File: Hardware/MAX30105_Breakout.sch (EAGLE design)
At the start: 27 parts, among them Q1 200mA/50V, Q2 200mA/50V, U1 1.8V/100mA, U2 MAX30105

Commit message: adding silk labelling
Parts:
- removed JP2: INT, SparkFun-Passives:JUMPER-PAD-2-NC_BY_TRACE
- removed JP3: PU, SparkFun-Passives:JUMPER-PAD-3-NC_BY_TRACE
- removed LOGO1: SFE_LOGO_NAME_FLAME.1_INCH, SparkFun-Aesthetics:SFE_LOGO_NAME_FLAME.1_INCH
- removed LOGO4: SFE_LOGO_FLAME.1EXP, SparkFun-Aesthetics:SFE_LOGO_FLAME.1EXP
- removed STANDOFF1, STANDOFF4: STAND-OFF, SparkFun-Electromechanical:STAND-OFF
- added FID3, FID4: FIDUCIALUFIDUCIAL, SparkFun-Aesthetics:FIDUCIALUFIDUCIAL
- added J1, J3, J4, J5, J6, J7, J8: GATORGATOR_MINI, SparkFun-Connectors:GATORGATOR_MINI
- FID1, FID2: value FIDUCIAL1X2 -> FIDUCIALUFIDUCIAL; device SparkFun-Aesthetics:FIDUCIAL1X2 -> SparkFun-Aesthetics:FIDUCIALUFIDUCIAL
- J2: value (none) -> GATORGATOR_MINI; device SparkFun-Connectors:M05PTH -> SparkFun-Connectors:GATORGATOR_MINI
- R1, R2: value 4.7K -> 10k; device SparkFun-Resistors:4.7KOHM-1/10W-1%(0603) -> SparkFun-Resistors:10KOHM-0603-1/10W-1%
- R8, R9: value 4.7K -> 2.2k; device SparkFun-Resistors:4.7KOHM-1/10W-1%(0603) -> SparkFun-Resistors:2.2KOHM-0603-1/10W-1%
- U2: value MAX30105 -> 30102; device SparkFun-Sensors:MAX30105SMD -> SparkFun-Sensors:MAX3010X-30102
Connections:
- removed net 5V: C1.1, C5.1, J2.3, JP2.2, JP3.2, U1.EN, U1.IN, U2.VLED+@10, U2.VLED+@9
- removed net N$1: JP2.1, R5.2
- removed net N$2: JP3.1, R2.2
- removed net N$3: JP3.3, R1.2
- new net 3.3V: C1.1, C5.1, J2.P$1, J6.P$1, R1.2, R2.2, R5.2, U1.EN, U1.IN, U2.VLED+@10, U2.VLED+@9
- net !INT: no longer J2.5
- net GND: now also J1.P$1, J5.P$1; no longer J2.4
- net SCL: now also J4.P$1, J8.P$1; no longer J2.1
- net SDA: now also J3.P$1, J7.P$1; no longer J2.2
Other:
- note removed: "Clear Jumper to remove I2C Pull-ups from bus"

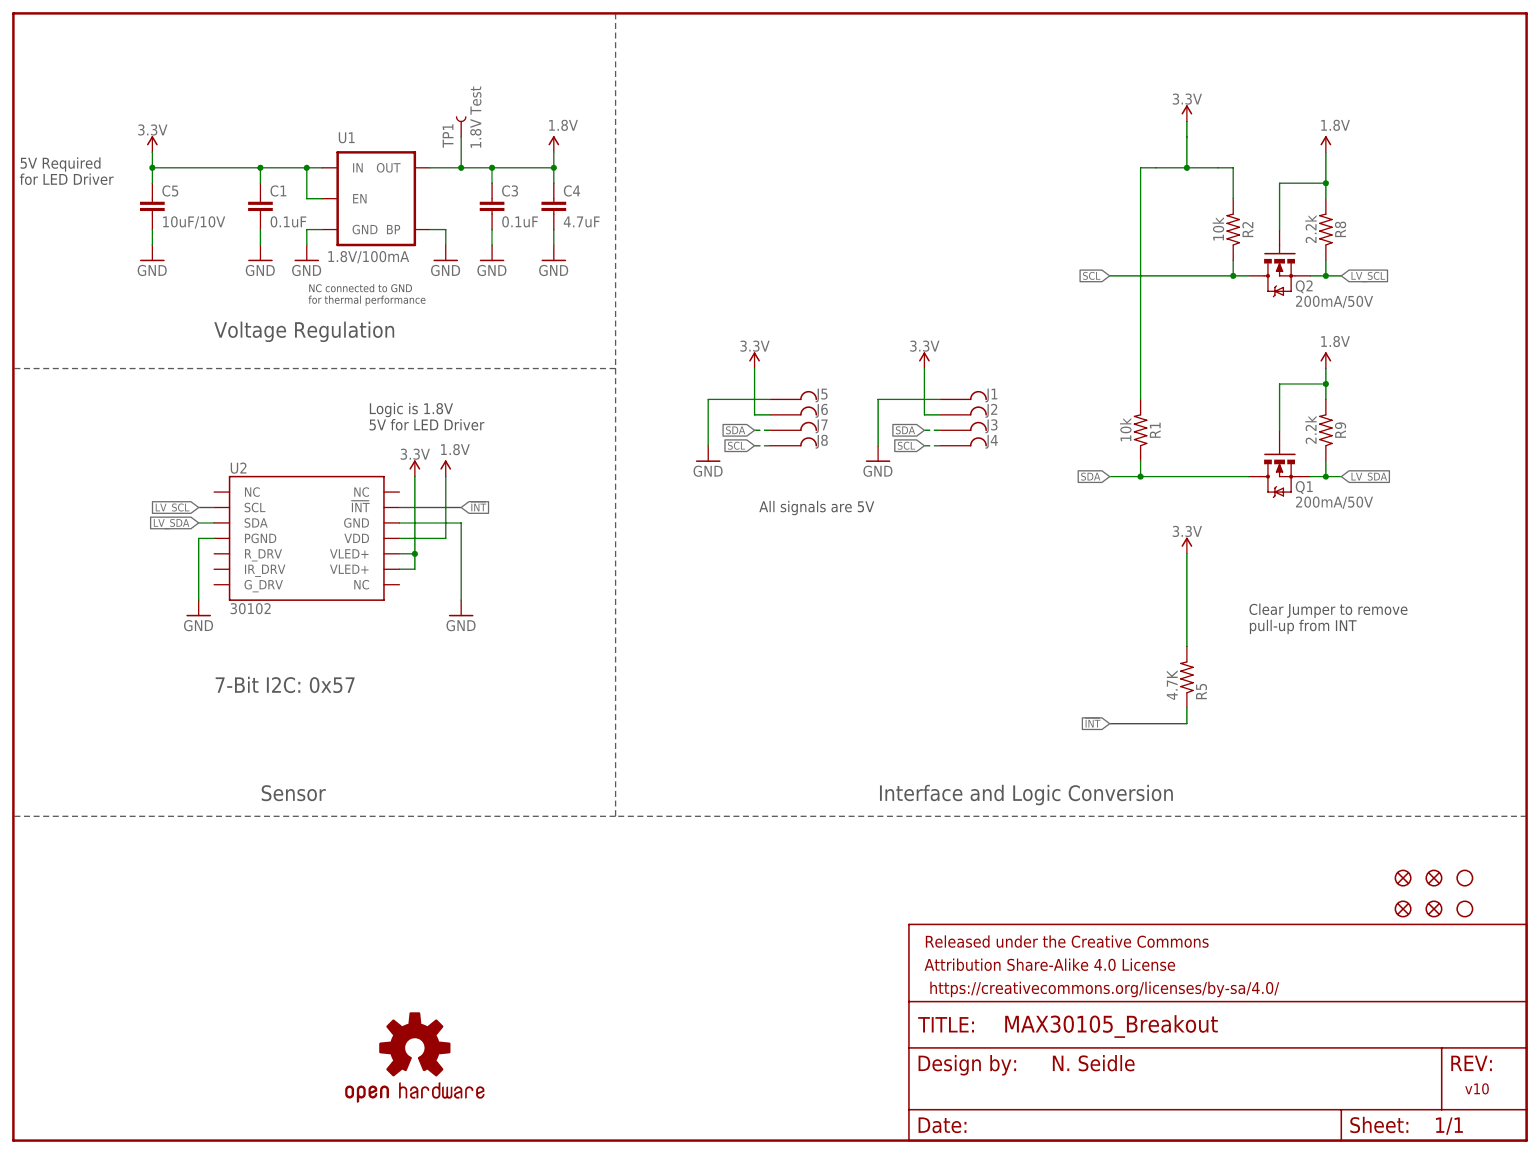
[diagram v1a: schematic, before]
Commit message: adding protection circuitry
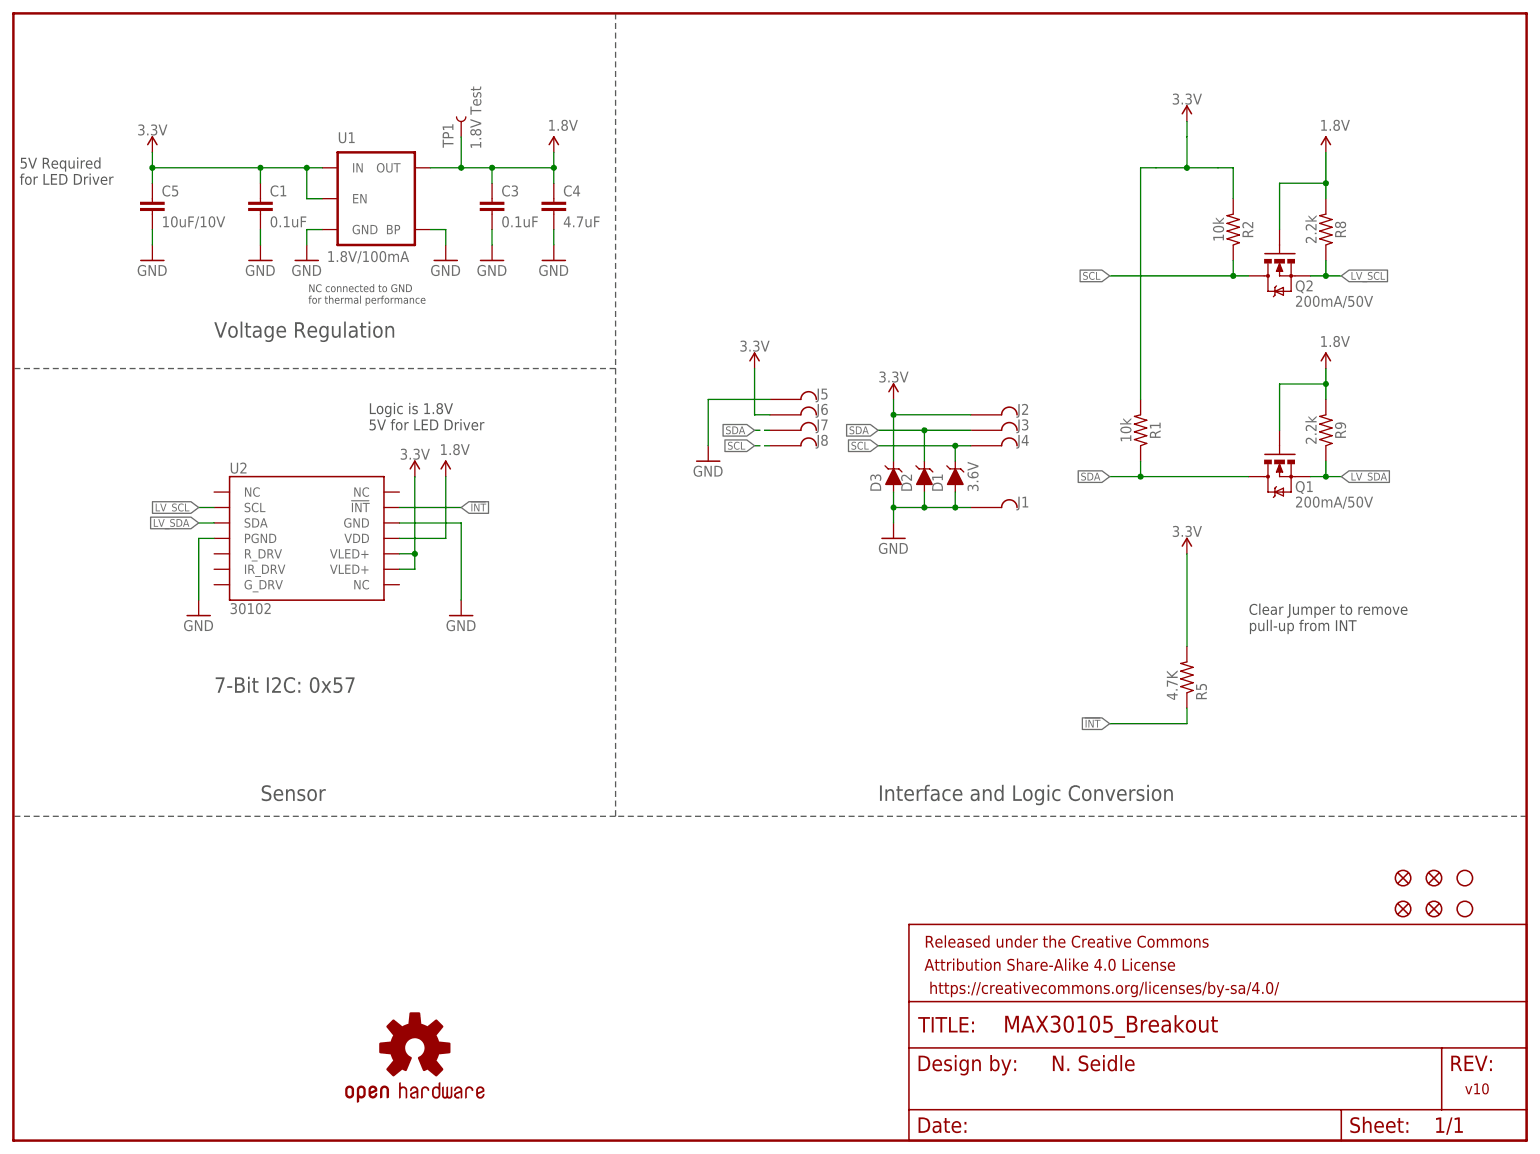
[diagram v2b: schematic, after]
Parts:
- added D1, D2, D3: 3.6V, SparkFun-DiscreteSemi:DIODE-ZENER-BZT52C3V6S
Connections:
- net 3.3V: now also D3.C
- net GND: now also D1.A, D2.A, D3.A
- net SCL: now also D1.C
- net SDA: now also D2.C
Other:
- note removed: "All signals are 5V"
- moved on the sheet: J1, J2, J3, J4

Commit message: finalizing silk and schematic before design review
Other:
- note added: "3.3V Required for LED Driver"
- note removed: "5V Required for LED Driver"
- note removed: "Clear Jumper to remove pull-up from INT"
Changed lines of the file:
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@@
 <?xml version="1.0" encoding="utf-8"?>
 <!DOCTYPE eagle SYSTEM "eagle.dtd">
-<eagle version="9.3.1">
+<eagle version="9.1.0">
 <drawing>
 <settings>
@@
 <text x="142.24" y="55.88" size="2.54" layer="97" font="vector">Interface and Logic Conversion</text>
 <text x="40.64" y="55.88" size="2.54" layer="97" font="vector">Sensor</text>
-<text x="1.016" y="157.226" size="1.778" layer="97" font="vector">5V Required
+<text x="1.016" y="157.226" size="1.778" layer="97" font="vector">3.3V Required
 for LED Driver</text>
-<text x="203.2" y="83.82" size="1.778" layer="97" font="vector">Clear Jumper to remove
-pull-up from INT</text>
 <text x="58.42" y="116.84" size="1.778" layer="97" font="vector">Logic is 1.8V
 5V for LED Driver</text>
@@
 <attribute name="VALUE" x="189.738" y="72.39" size="1.778" layer="96" rot="MR90"/>
 </instance>
-<instance part="SUPPLY5" gate="G$1" x="193.04" y="96.52" smashed="yes">
-<attribute name="VALUE" x="193.04" y="99.314" size="1.778" layer="96" align="bottom-center"/>
+<instance part="SUPPLY5" gate="G$1" x="193.04" y="83.82" smashed="yes">
+<attribute name="VALUE" x="193.04" y="86.614" size="1.778" layer="96" align="bottom-center"/>
 </instance>
 <instance part="SUPPLY9" gate="G$1" x="66.04" y="109.22" smashed="yes">
@@
 <segment>
 <pinref part="SUPPLY5" gate="G$1" pin="3.3V"/>
-<wire x1="193.04" y1="96.52" x2="193.04" y2="81.28" width="0.1524" layer="91"/>
+<wire x1="193.04" y1="83.82" x2="193.04" y2="81.28" width="0.1524" layer="91"/>
 <pinref part="R5" gate="G$1" pin="2"/>
 </segment>

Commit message: engineer run of checklist
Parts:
- added D4: RED, SparkFun-LED:LED-RED0603
- added Q3: 2.5A/30V/105mΩ, SparkFun-DiscreteSemi:MOSFET_PCH-DMG2307L
- added R3, R4: 10k, SparkFun-Resistors:10KOHM-0603-1/10W-1%
- C1, C3: device SparkFun-Capacitors:0.1UF-25V(+80/-20%)(0603) -> SparkFun-Capacitors:0.1UF-0603-25V-(+80/-20%)
- C4: device SparkFun-Capacitors:4.7UF-6.3V-10%(0603)0603 -> SparkFun-Capacitors:4.7UF-0603-6.3V-(10%)
- C5: value 10uF/10V -> 10uF; device SparkFun-Capacitors:10UF10V10%(0805) -> SparkFun-Capacitors:10UF-0603-6.3V-20%
- R5: value 4.7K -> 4.7k; device SparkFun-Resistors:4.7KOHM-1/10W-1%(0603) -> SparkFun-Resistors:4.7KOHM-0603-1/10W-1%
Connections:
- new net N$1: D3.A, Q3.G, R3.2
- new net N$2: J2.P$1, J6.P$1, Q3.D
- new net N$3: D4.C, R4.2
- net 3.3V: now also D4.A, Q3.S; no longer J2.P$1, J6.P$1
- net GND: now also R3.1, R4.1; no longer D3.A
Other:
- note added: "A. England"
- note removed: "N. Seidle"
- moved on the sheet: D1, D2, D3, J1, J2, J3, J4, J5, J6, J7, J8

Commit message: forgot to save changes from review/checklist
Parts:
- added LOGO1: SFE_LOGO_NAME_FLAME.1_INCH, SparkFun-Aesthetics:SFE_LOGO_NAME_FLAME.1_INCH
- Q1, Q2: value 200mA/50V -> 220mA/50V/3.5Ω; device SparkFun-DiscreteSemi:MOSFET-NCHANNELBSS138 -> SparkFun-DiscreteSemi:MOSFET-NCH-BSS138
- STANDOFF2, STANDOFF3: value STAND-OFF -> STAND-OFFTIGHT; device SparkFun-Electromechanical:STAND-OFF -> SparkFun-Hardware:STAND-OFFTIGHT
- U1: device SparkFun-PowerIC:V_REG_SP62141.8V -> SparkFun-IC-Power:V_REG_SP6214-1.8V
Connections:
- net GND: now also U1.NC; no longer U1.BP
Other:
- note added: "Logic is 1.8V 3.3V for LED Driver"
- note added: "VIN: 3-7V"
- note added: "v01"
- note removed: "Logic is 1.8V 5V for LED Driver"
- note removed: "v10"
- moved on the sheet: R2
